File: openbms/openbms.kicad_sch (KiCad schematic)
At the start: 0 parts

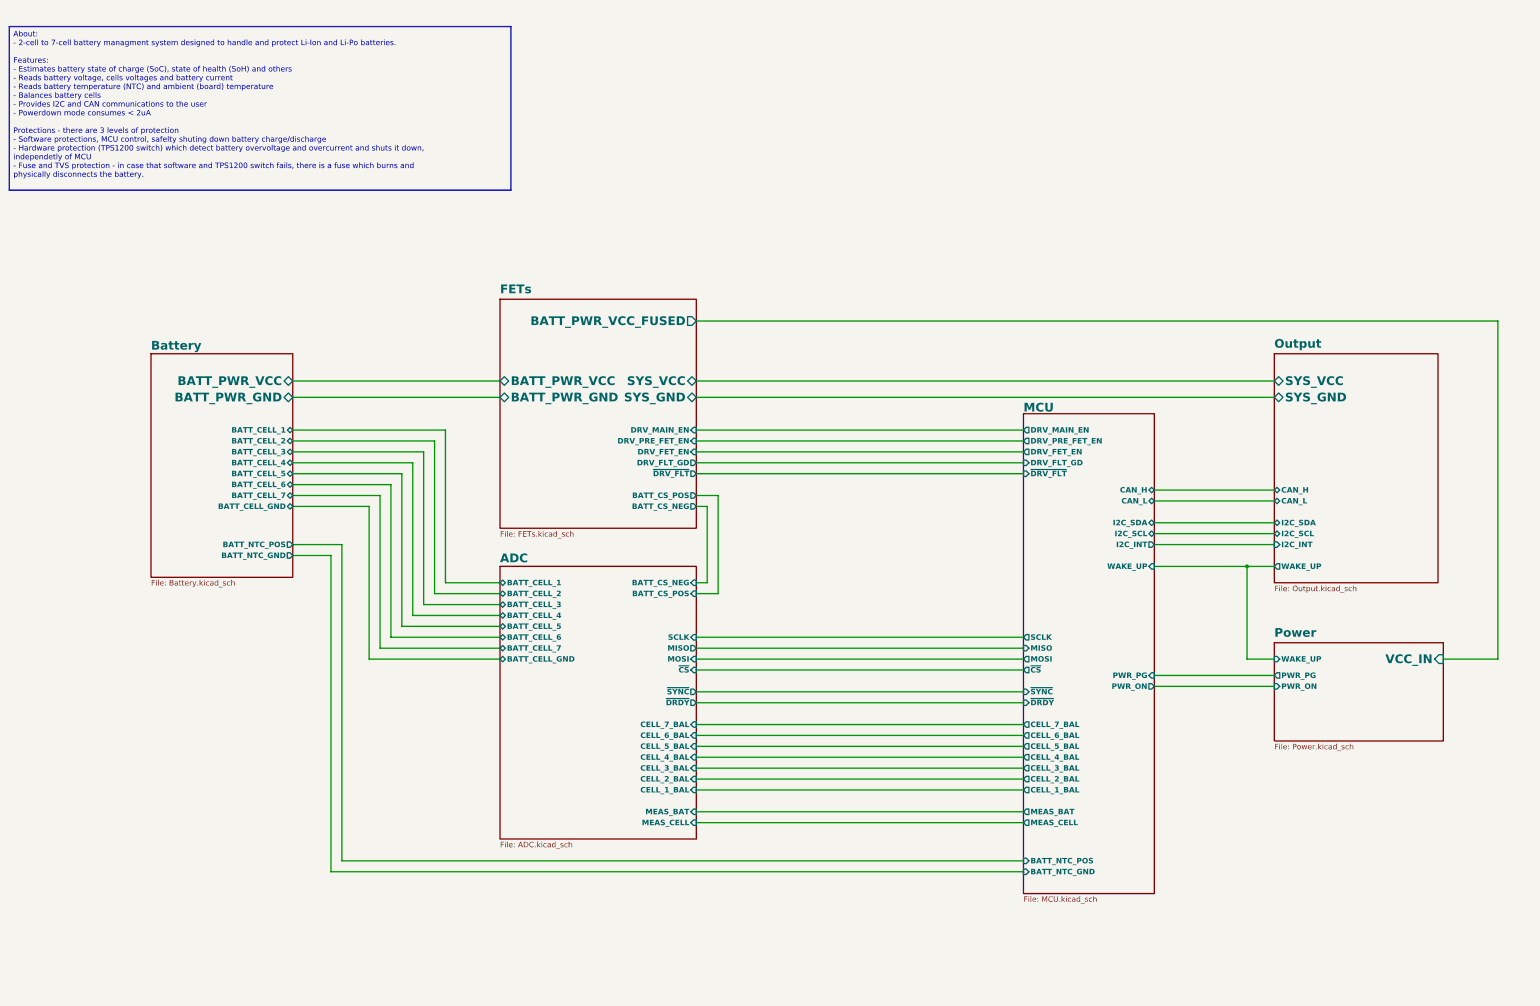
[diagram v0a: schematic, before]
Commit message: Footprints for pmos/nmos and pmos/pmos packages fixed, charger detection added, pwr_gd and flt_gd lines removed
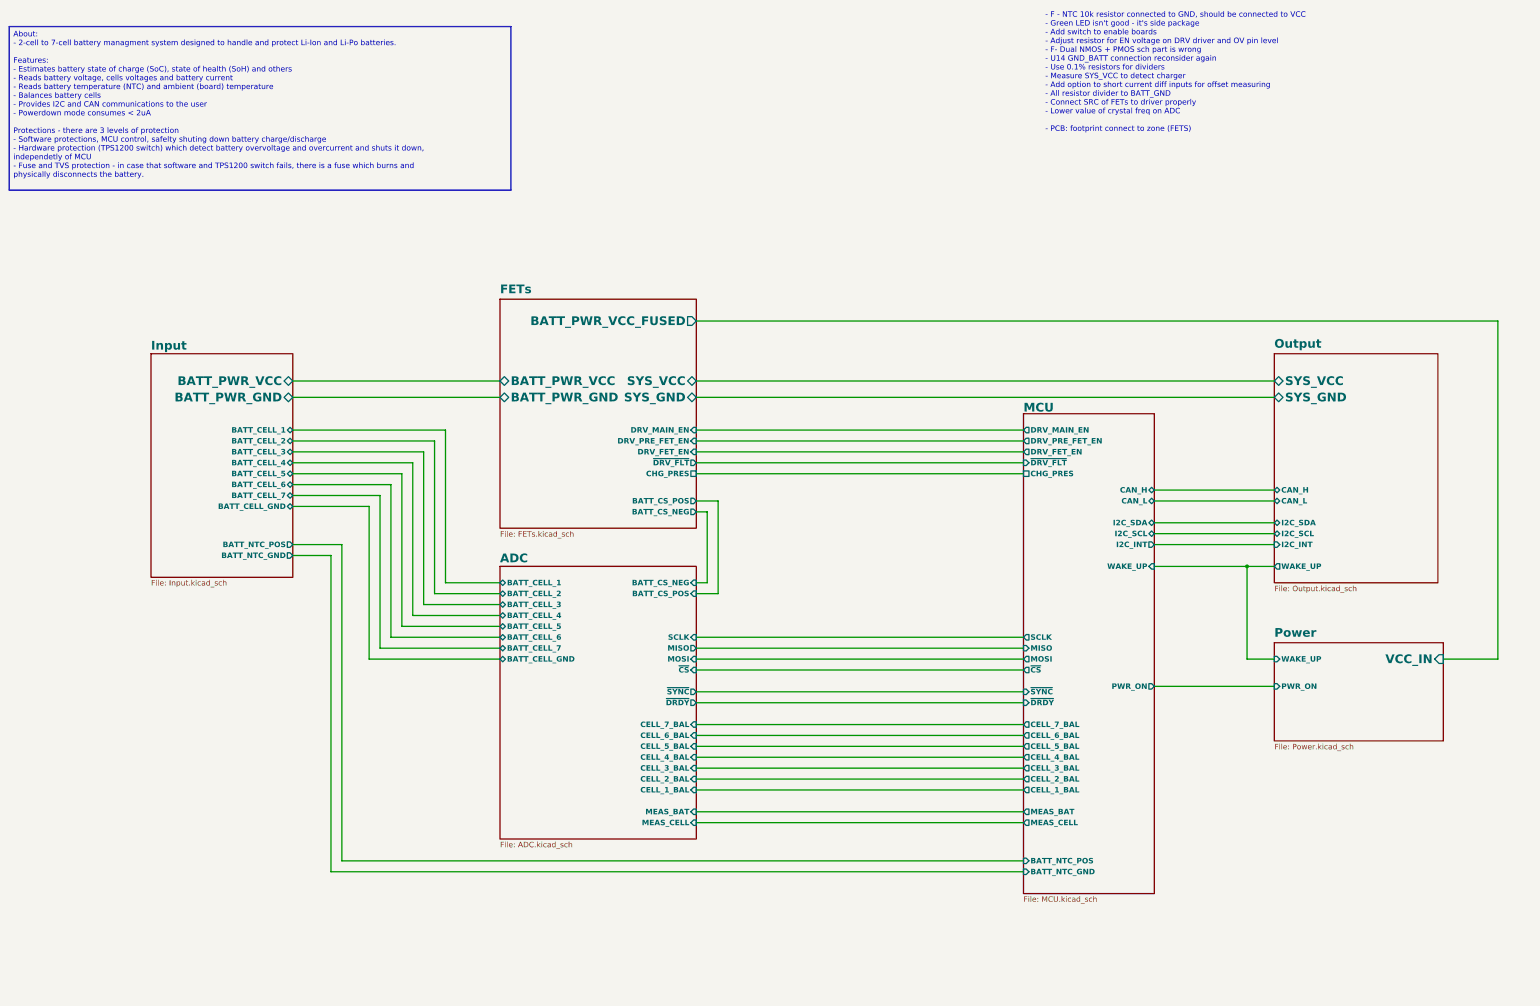
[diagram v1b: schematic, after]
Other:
- sheet Battery renamed Input
- sheet FETs ports: added CHG_PRES; removed DRV_FLT_GD
- sheet Input: file Battery.kicad_sch -> Input.kicad_sch
- sheet MCU ports: added CHG_PRES; removed DRV_FLT_GD, PWR_PG
- sheet Power ports: added none; removed PWR_PG
- note added: "- F - NTC 10k resistor connected to GND, should be connected to VCC - Green LED isn't good - it's side package - Add switch to enable boards - Adjust resistor for EN voltage on DRV driver and OV pin level - F- Dual NMOS + PMOS sch part is wrong - U14 GND_BATT connection reconsider again - Use 0.1% resistors for dividers - Measure SYS_VCC to detect charger - Add option to short current diff inputs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"
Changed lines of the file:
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@@
 		(comment 4 "Open Source Battery Management System")
+	)
+	(text "- F - NTC 10k resistor connected to GND, should be connected to VCC\n- Green LED isn't good - it's side package\n- Add switch to enable boards\n- Adjust resistor for EN voltage on DRV driver and OV pin level\n- F- Dual NMOS + PMOS sch part is wrong\n- U14 GND_BATT connection reconsider again\n- Use 0.1% resistors for dividers\n- Measure SYS_VCC to detect charger\n- Add option to short current diff inputs for offset measuring\n- All resistor divider to BATT_GND\n- Connect SRC of FETs to driver properly\n- Lower value of crystal freq on ADC\n\n- PCB: footprint connect to zone (FETS)\n"
+		(exclude_from_sim no)
+		(at 259.08 28.448 0)
+		(effects
+			(font
+				(size 1.27 1.27)
+				(color 255 0 0 1)
+			)
+			(justify left)
+		)
 	)
 	(text_box "About:\n- 2-cell to 7-cell battery managment system designed to handle and protect Li-Ion and Li-Po batteries.\n\nFeatures:\n- Estimates battery state of charge (SoC), state of health (SoH) and others\n- Reads battery voltage, cells voltages and battery current\n- Reads battery temperature (NTC) and ambient (board) temperature\n- Balances battery cells\n- Provides I2C and CAN communications to the user\n- Powerdown mode consumes < 2uA\n\nProtections - there are 3 levels of protection\n- Software protections, MCU control, safelty shuting down battery charge/discharge\n- Hardware protection (TPS1200 switch) which detect battery overvoltage and overcurrent and shuts it down, independetly of MCU\n- Fuse and TVS protection - in case that software and TPS1200 switch fails, there is a fuse which burns and physically disconnects the battery.\n"
@@
 	(wire
 		(pts
-			(xy 177.8 129.54) (xy 180.34 129.54)
+			(xy 177.8 130.81) (xy 180.34 130.81)
 		)
 		(stroke
@@
 	(wire
 		(pts
+			(xy 177.8 121.92) (xy 254 121.92)
+		)
+		(stroke
+			(width 0.3048)
+			(type default)
+			(color 0 0 132 1)
+		)
+	)
+	(wire
+		(pts
 			(xy 106.68 160.02) (xy 132.08 160.02)
 		)
@@
 		(pts
 			(xy 306.07 143.51) (xy 312.42 143.51)
-		)
-		(stroke
-			(width 0.3048)
-			(type default)
-			(color 132 0 0 1)
-		)
-	)
-	(wire
-		(pts
-			(xy 284.48 168.91) (xy 312.42 168.91)
 		)
 		(stroke
@@
 	(wire
 		(pts
-			(xy 180.34 129.54) (xy 180.34 147.32)
+			(xy 180.34 130.81) (xy 180.34 147.32)
 		)
 		(stroke
@@
 	(wire
 		(pts
-			(xy 182.88 149.86) (xy 182.88 127)
+			(xy 182.88 149.86) (xy 182.88 128.27)
 		)
 		(stroke
@@
 	(wire
 		(pts
-			(xy 177.8 119.38) (xy 254 119.38)
-		)
-		(stroke
-			(width 0.3048)
-			(type default)
-			(color 0 0 132 1)
-		)
-	)
-	(wire
-		(pts
 			(xy 83.82 100.33) (xy 132.08 100.33)
 		)
@@
 	(wire
 		(pts
-			(xy 177.8 121.92) (xy 254 121.92)
+			(xy 177.8 119.38) (xy 254 119.38)
 		)
 		(stroke
@@
 	(wire
 		(pts
-			(xy 182.88 127) (xy 177.8 127)
+			(xy 182.88 128.27) (xy 177.8 128.27)
 		)
 		(stroke
@@
 			)
 		)
-		(pin "DRV_FLT_GD" input
-			(at 254 119.38 180)
-			(effects
-				(font
-					(size 1.27 1.27)
-					(thickness 0.254)
-					(bold yes)
-					(color 0 0 132 1)
-				)
-				(justify left)
-			)
-		)
 		(pin "MISO" input
 			(at 254 162.56 180)
@@
 		)
 		(pin "~{DRV_FLT}" input
-			(at 254 121.92 180)
+			(at 254 119.38 180)
 			(effects
 				(font
@@
 			)
 		)
-		(pin "PWR_PG" input
-			(at 284.48 168.91 0)
-			(effects
-				(font
-					(size 1.27 1.27)
-					(thickness 0.254)
-					(bold yes)
-					(color 132 0 0 1)
-				)
-				(justify right)
-			)
-		)
 		(pin "PWR_ON" output
 			(at 284.48 171.45 0)
@@
 				)
 				(justify right)
+			)
+		)
+		(pin "CHG_PRES" passive
+			(at 254 121.92 180)
+			(effects
+				(font
+					(size 1.27 1.27)
+					(thickness 0.254)
+					(bold yes)
+					(color 0 0 132 1)
+				)
+				(justify left)
 			)
 		)
@@
 			(color 0 0 0 0.0000)
 		)
-		(property "Sheetname" "Battery"
+		(property "Sheetname" "Input"
 			(at 50.8 93.2684 0)
 			(effects
@@
 			)
 		)
-		(property "Sheetfile" "Battery.kicad_sch"
+		(property "Sheetfile" "Input.kicad_sch"
 			(at 50.8 146.6346 0)
 			(effects
@@
 			)
 		)
-		(pin "PWR_PG" output
-			(at 312.42 168.91 180)
-			(effects
-				(font
-					(size 1.27 1.27)
-					(thickness 0.254)
-					(bold yes)
-					(color 132 0 0 1)
-				)
-				(justify left)
-			)
-		)
 		(pin "PWR_ON" input
 			(at 312.42 171.45 180)
@@
 			)
 		)
-		(pin "DRV_FLT_GD" output
+		(pin "~{DRV_FLT}" output
 			(at 177.8 119.38 0)
-			(effects
-				(font
-					(size 1.27 1.27)
-					(thickness 0.254)
-					(bold yes)
-					(color 0 0 132 1)
-				)
-				(justify right)
-			)
-		)
-		(pin "~{DRV_FLT}" output
-			(at 177.8 121.92 0)
 			(effects
 				(font
@@
 		)
 		(pin "BATT_CS_NEG" output
-			(at 177.8 129.54 0)
+			(at 177.8 130.81 0)
 			(effects
 				(font
@@
 		)
 		(pin "BATT_CS_POS" output
-			(at 177.8 127 0)
+			(at 177.8 128.27 0)
 			(effects
 				(font
@@
 				)
 				(justify right)
+			)
+		)
+		(pin "CHG_PRES" passive
+			(at 177.8 121.92 0)
+			(effects
+				(font
+					(size 1.27 1.27)
+					(thickness 0.254)
+					(bold yes)
+					(color 0 0 132 1)
+				)
+				(justify right)

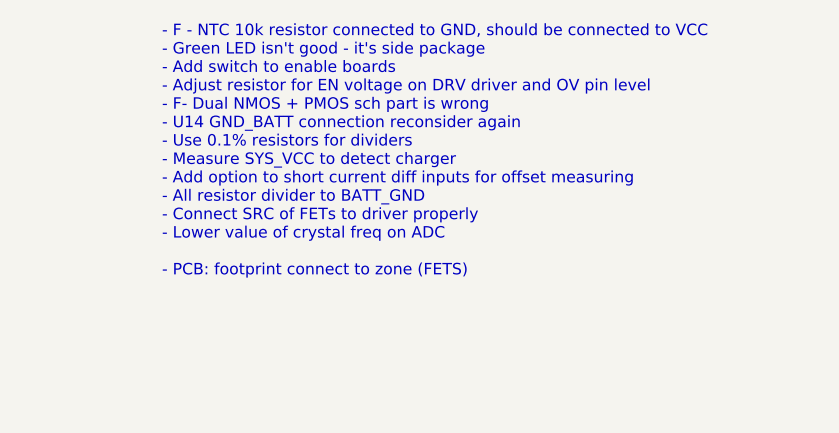
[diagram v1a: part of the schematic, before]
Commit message: Resistor dividers updated and put to 0.1% tolerance
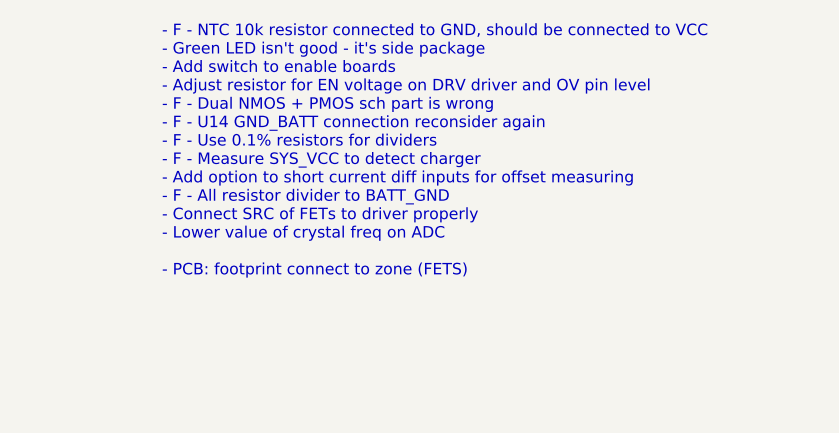
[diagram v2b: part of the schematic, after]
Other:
- note added: "- F - NTC 10k resistor connected to GND, should be connected to VCC - Green LED isn't good - it's side package - Add switch to enable boards - Adjust resistor for EN voltage on DRV driver and OV pin level - F - Dual NMOS + PMOS sch part is wrong - F - U14 GND_BATT connection reconsider again - F - Use 0.1% resistors for dividers - F - Measure SYS_VCC to detect charger - Add option to short curren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"
- note removed: "- F - NTC 10k resistor connected to GND, should be connected to VCC - Green LED isn't good - it's side package - Add switch to enable boards - Adjust resistor for EN voltage on DRV driver and OV pin level - F- Dual NMOS + PMOS sch part is wrong - U14 GND_BATT connection reconsider again - Use 0.1% resistors for dividers - Measure SYS_VCC to detect charger - Add option to short current diff inputs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"
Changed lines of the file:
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@@
 		(comment 4 "Open Source Battery Management System")
 	)
-	(text "- F - NTC 10k resistor connected to GND, should be connected to VCC\n- Green LED isn't good - it's side package\n- Add switch to enable boards\n- Adjust resistor for EN voltage on DRV driver and OV pin level\n- F- Dual NMOS + PMOS sch part is wrong\n- U14 GND_BATT connection reconsider again\n- Use 0.1% resistors for dividers\n- Measure SYS_VCC to detect charger\n- Add option to short current diff inputs for offset measuring\n- All resistor divider to BATT_GND\n- Connect SRC of FETs to driver properly\n- Lower value of crystal freq on ADC\n\n- PCB: footprint connect to zone (FETS)\n"
+	(text "- F - NTC 10k resistor connected to GND, should be connected to VCC\n- Green LED isn't good - it's side package\n- Add switch to enable boards\n- Adjust resistor for EN voltage on DRV driver and OV pin level\n- F - Dual NMOS + PMOS sch part is wrong\n- F - U14 GND_BATT connection reconsider again\n- F - Use 0.1% resistors for dividers\n- F - Measure SYS_VCC to detect charger\n- Add option to short current diff inputs for offset measuring\n- F - All resistor divider to BATT_GND\n- Connect SRC of FETs to driver properly\n- Lower value of crystal freq on ADC\n\n- PCB: footprint connect to zone (FETS)\n"
 		(exclude_from_sim no)
 		(at 259.08 28.448 0)
